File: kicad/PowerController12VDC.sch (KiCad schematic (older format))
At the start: 0 parts

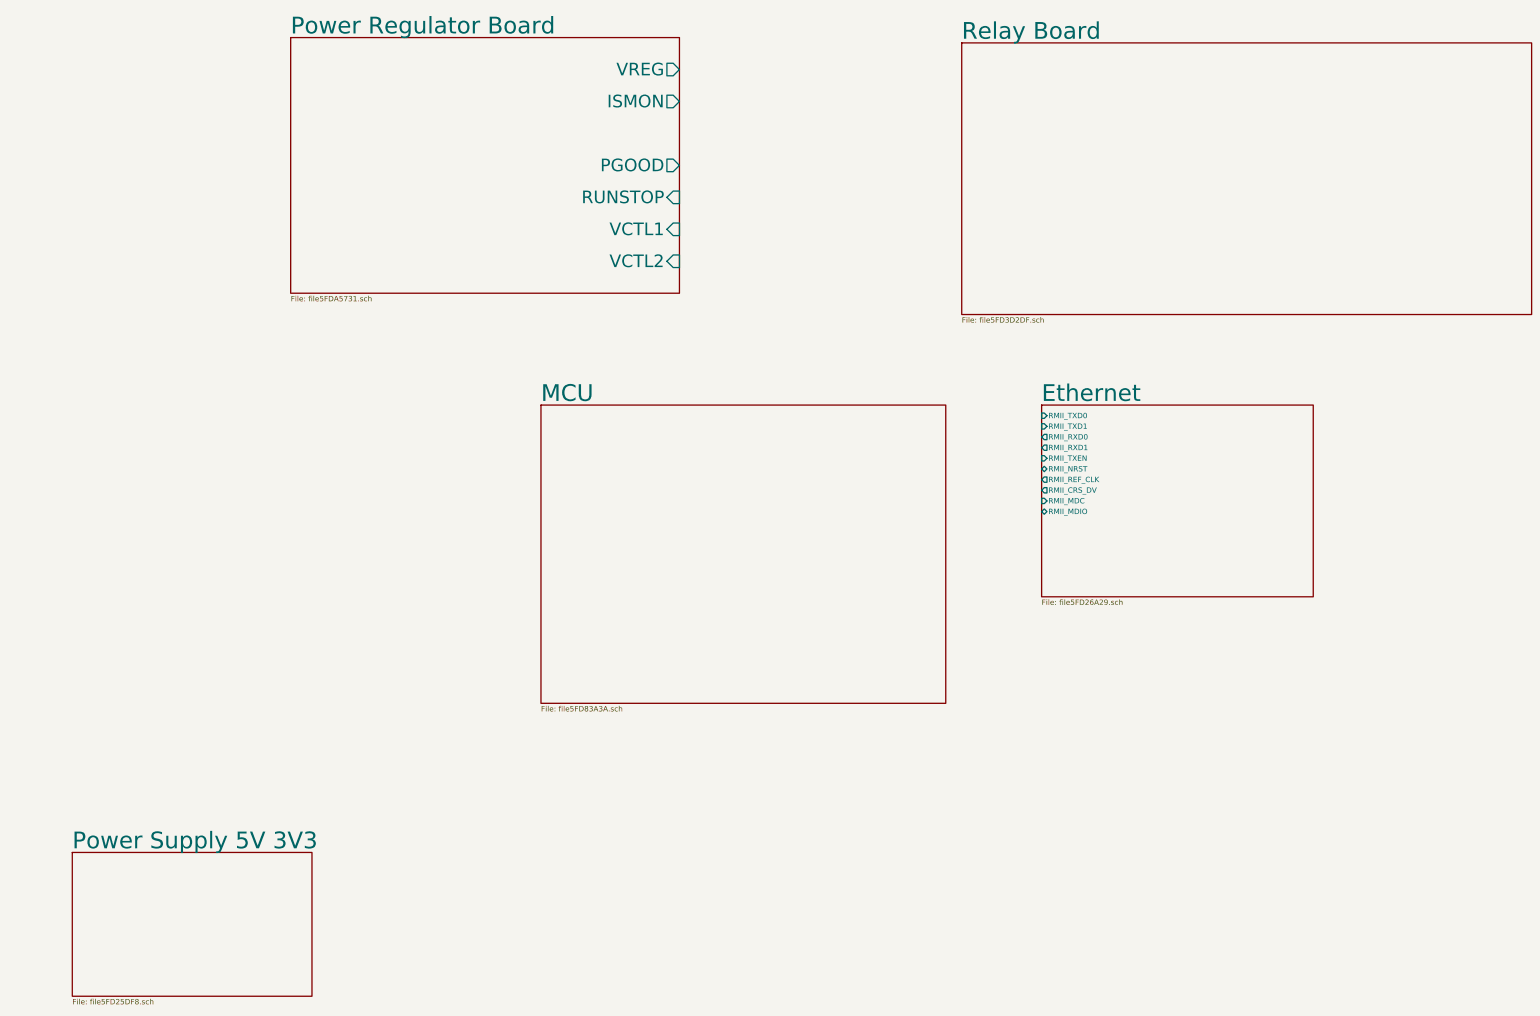
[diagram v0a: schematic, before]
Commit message: Add datasheets
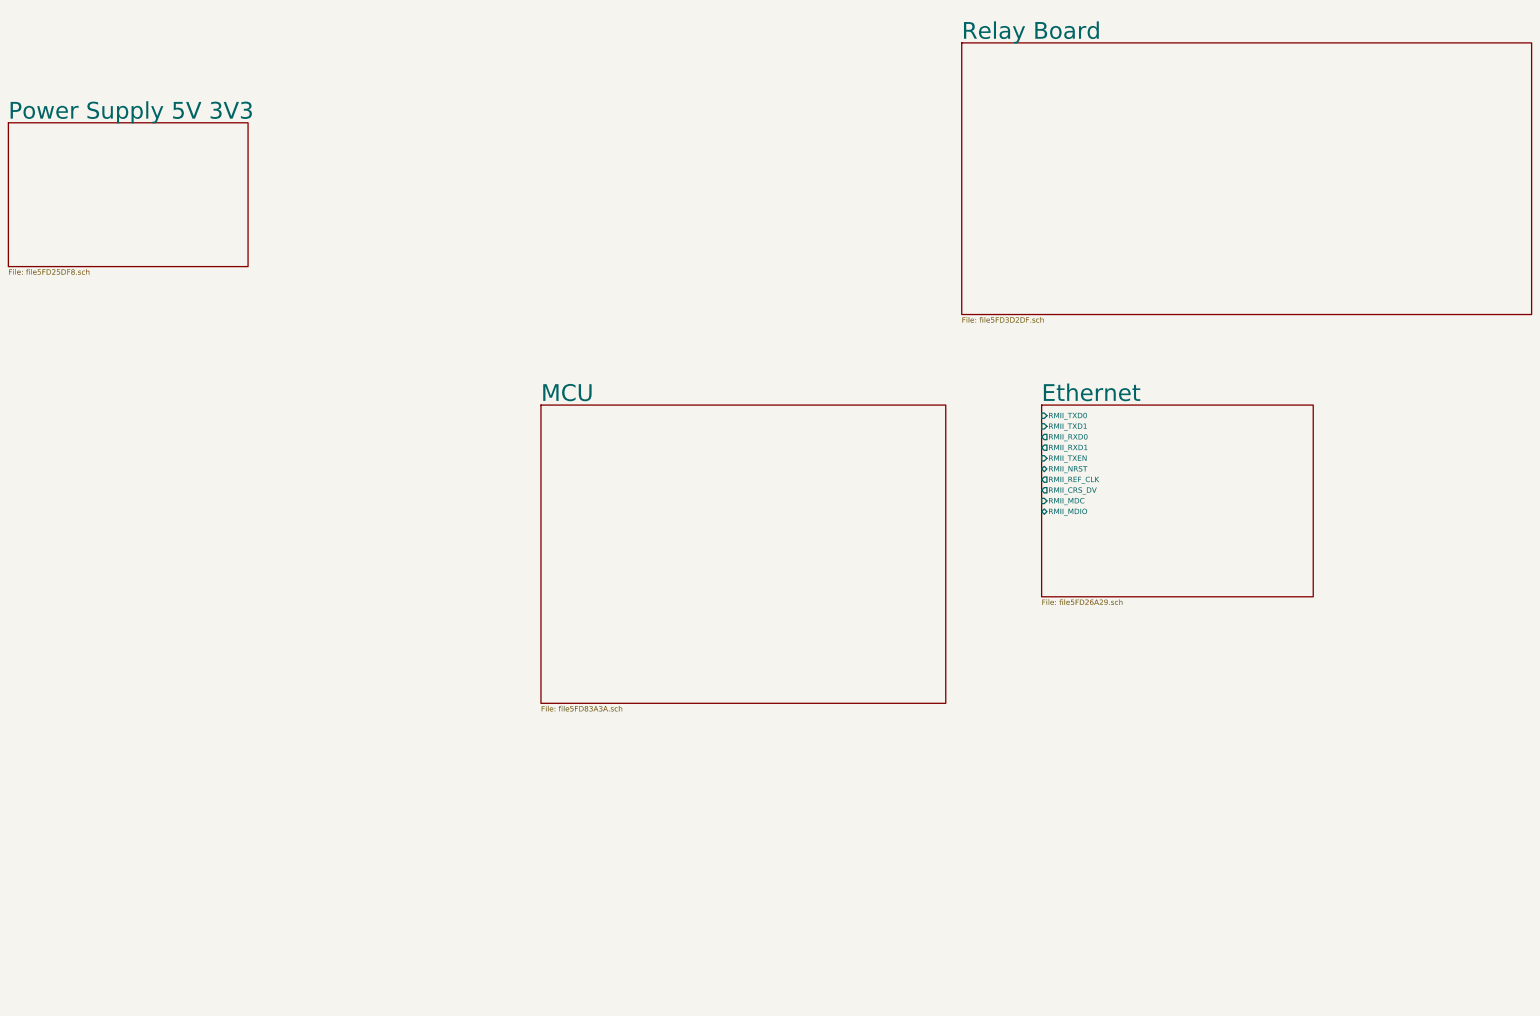
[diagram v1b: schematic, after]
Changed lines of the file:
@@
 $Descr USLedger 17000 11000
 encoding utf-8
-Sheet 1 6
+Sheet 1 5
 Title "KQ9P Power Controller 12VDC"
 Date "2020-12-08"
@@
 $EndDescr
 $Sheet
-S 2450 8650 2250 1350
+S 1850 1800 2250 1350
 U 5FD25DF9
 F0 "Power Supply 5V 3V3" 157
@@
 F1 "file5FD3D2DF.sch" 50
 $EndSheet
-$Sheet
-S 4500 1000 3650 2400
-U 5FDA5732
-F0 "Power Regulator Board" 157
-F1 "file5FDA5731.sch" 50
-F2 "PGOOD" O R 8150 2200 118
-F3 "VREG" O R 8150 1300 118
-F4 "ISMON" O R 8150 1600 118
-F5 "RUNSTOP" I R 8150 2500 118
-F6 "VCTL1" I R 8150 2800 118
-F7 "VCTL2" I R 8150 3100 118
-$EndSheet
 $EndSCHEMATC
